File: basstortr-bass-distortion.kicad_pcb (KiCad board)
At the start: 2 copper layers, 50 x 80 mm, 48 parts, among them J1 Conn_01x04_Pin, J2 Conn_01x02_Pin, J3 Conn_01x02_Pin, Q1 BS170, Q2 BS170, Q3 BS170

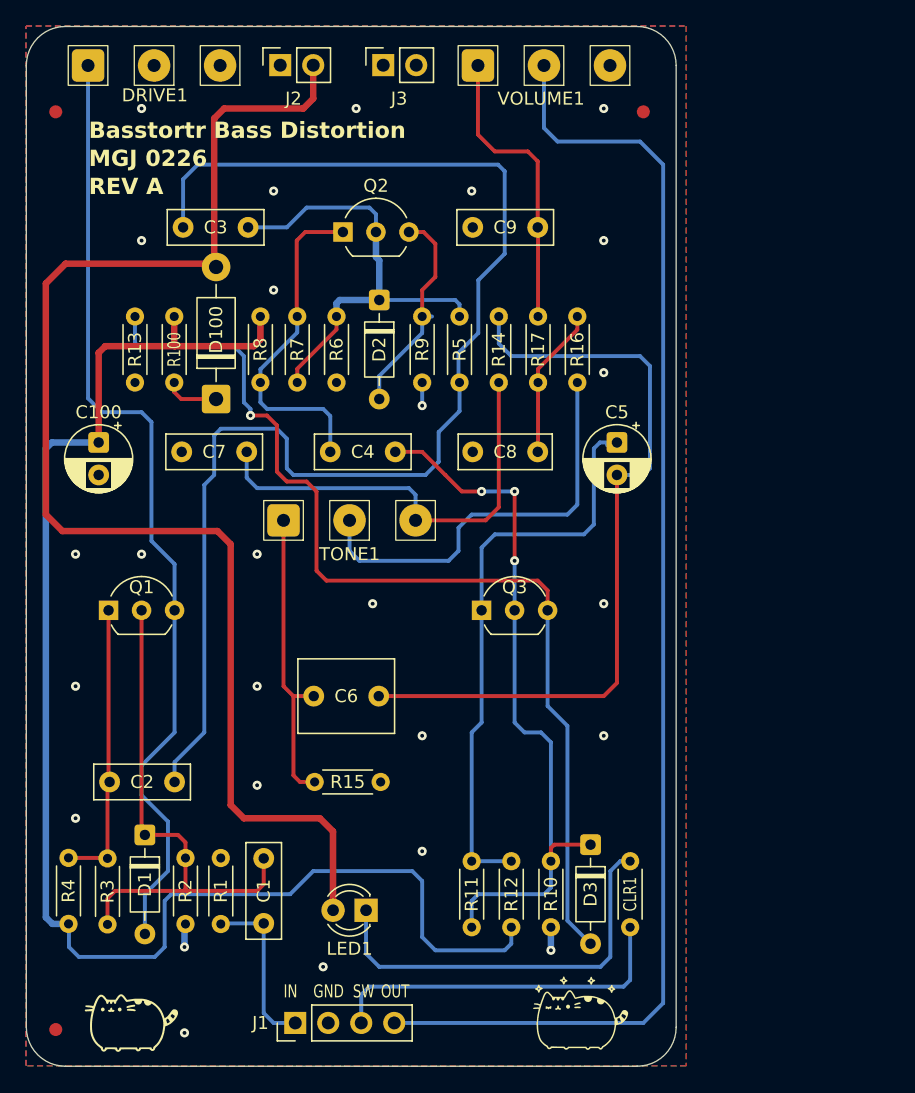
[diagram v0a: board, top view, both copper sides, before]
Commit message: RevB: New footprints and tracks
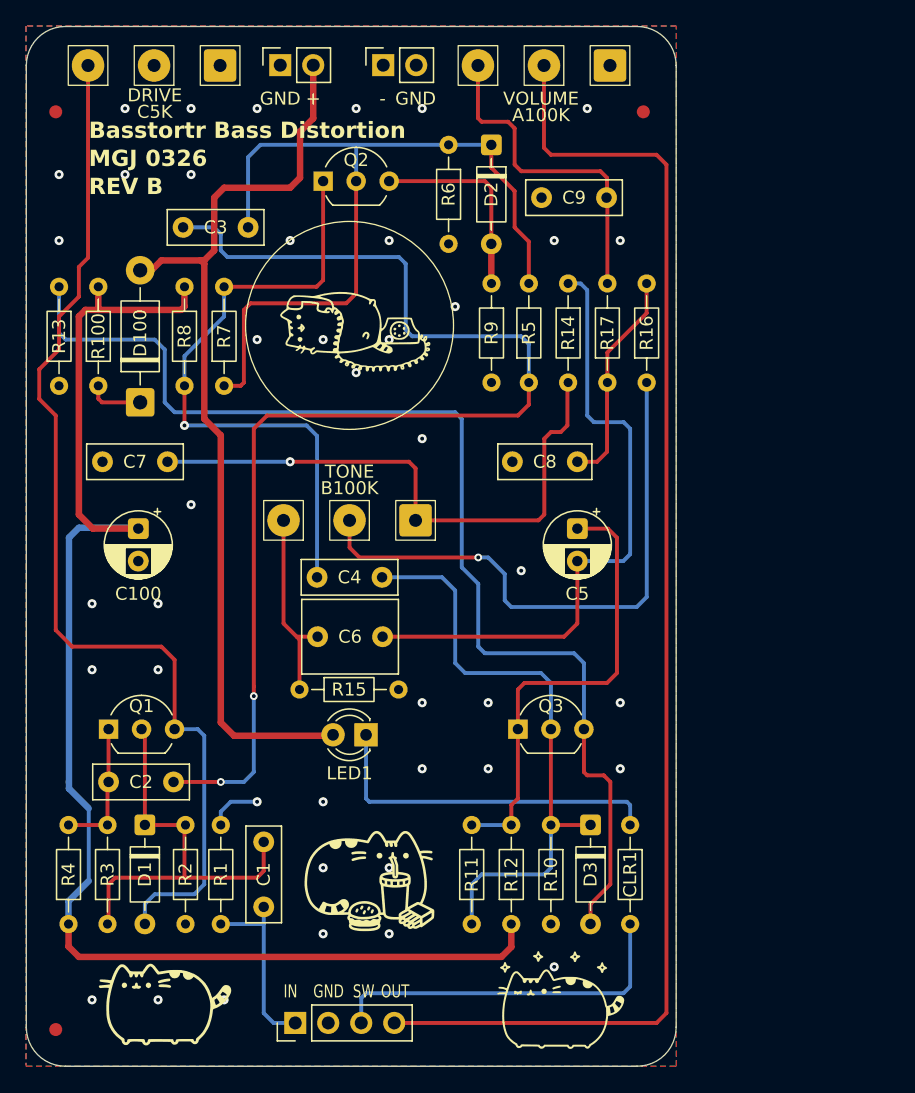
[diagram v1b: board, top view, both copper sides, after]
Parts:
- removed the G*** at (22.6, 90.1)
- removed the G*** at (57.1, 89.4)
- added G***: LOGO, LOGO, F.Cu at (40.9, 79.2)
- added G***: LOGO, LOGO, F.Cu at (39.9, 36.6)
- added G***: LOGO, LOGO, F.Cu at (55.6, 88.4)
- added G***: LOGO, LOGO, F.Cu at (25.1, 88.7)
- CLR1, R1, R10, R100, R11, R12, R13, R14, R15, R16, R17, R2, R3, R4, R5, R6, R7, R8, R9: footprint Resistor_THT:R_Axial_DIN0204_L3.6mm_D1.6mm_P5.08mm_Horizontal -> Resistor_THT:R_Axial_DIN0204_L3.6mm_D1.6mm_P7.62mm_Horizontal
- moved R6 15.8 mm to (47.0, 22.6)
- moved D2 14.7 mm to (50.3, 22.6)
- moved LED1 13.5 mm to (40.6, 68.0)
- moved C4 9.71 mm to (36.9, 55.9)
- moved Q3 9.56 mm to (52.3, 67.6)
- moved Q1 9.14 mm to (20.8, 67.6)
- moved C100 7.30 mm to (23.1, 52.1)
- moved C5 7.30 mm to (56.9, 52.1)
- moved R15 7.21 mm to (35.5, 64.5)
- moved R13 6.27 mm to (17.0, 33.5)
- moved R8 6.27 mm to (26.7, 33.5)
- moved C7 6.14 mm to (20.4, 47.0)
- moved R14 5.91 mm to (56.2, 33.3)
- moved R9 5.91 mm to (50.3, 33.3)
- moved D100 5.85 mm to (23.3, 42.4)
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- renumbered DRIVE1 to DRIVE, TONE1 to TONE, VOLUME1 to VOLUME
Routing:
- net /+: track 103.9 -> 72.0 mm
- net Net-(D2-K): track 35.4 -> 64.2 mm
- net Net-(Q2-D): track 26.0 -> 48.8 mm, vias 0 -> 1
- net Net-(R16-Pad1): track 32.4 -> 44.9 mm, vias 0 -> 1
- net Net-(Q1-D): track 22.2 -> 10.4 mm
- net Net-(C7-Pad2): track 33.9 -> 44.8 mm, vias 0 -> 1
- net Net-(C5-Pad2): track 59.8 -> 49.2 mm
- net Net-(D3-A): track 78.3 -> 88.6 mm, vias 1 -> 0
- net Net-(Q3-D): track 45.0 -> 35.6 mm
- net Net-(D3-K): track 55.5 -> 46.6 mm, vias 3 -> 0
- net Net-(C2-Pad2): track 102.3 -> 93.5 mm, vias 0 -> 2
- net Net-(D1-K): track 41.0 -> 32.4 mm
- net Net-(C6-Pad1): track 23.3 -> 15.1 mm
- net Net-(D1-A): track 74.0 -> 81.6 mm
- net VCC: track 113.6 -> 106.9 mm
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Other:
- board text added: "+"
- board text added: "-"
- board text added: "A100K"
- board text added: "B100K"
- board text added: "C5K"
- board text added: "MGJ 0326"
- board text added: "REV B"
- board text removed: "MGJ 0226"
- board text removed: "REV A"

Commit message: Rev C: Isolating parts to fit inside 125B
Fixed trace widths, trying to trace out signal on only one layer, changed component placement, etc..
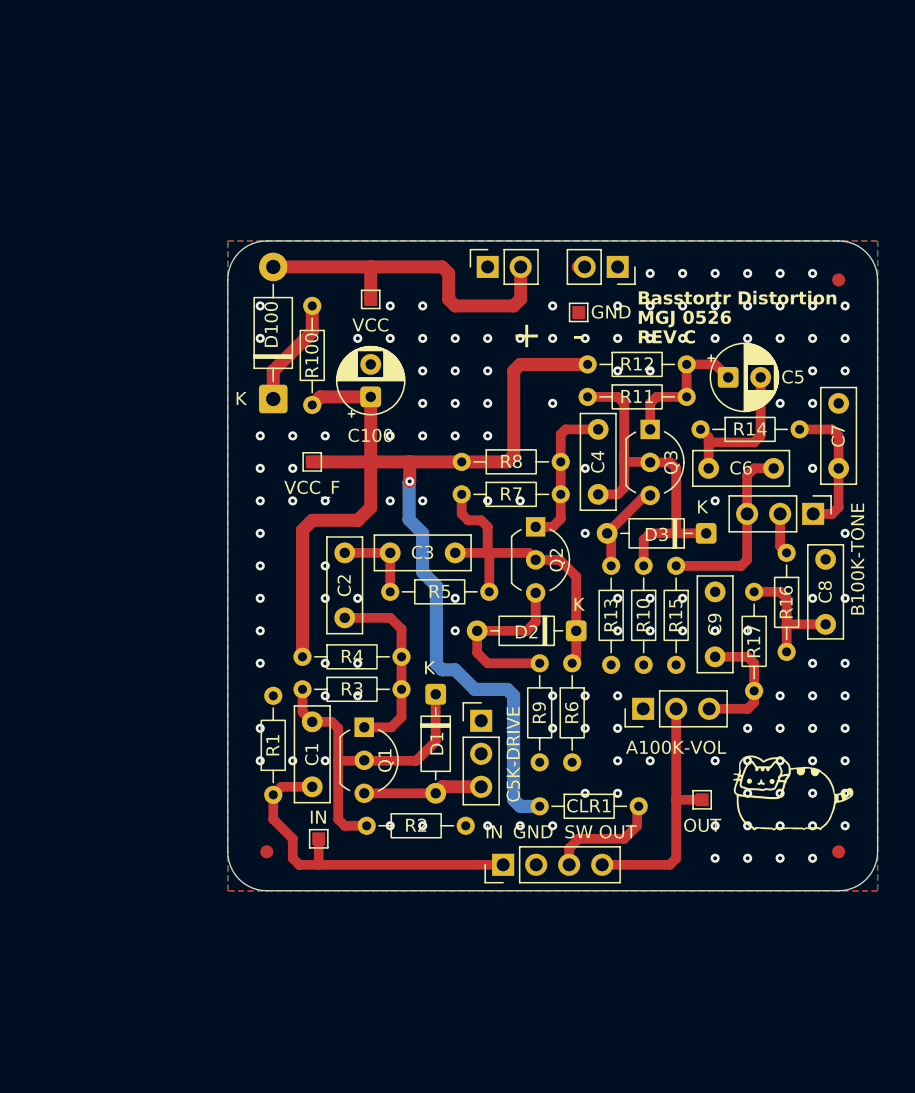
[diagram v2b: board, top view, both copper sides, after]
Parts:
- removed DRIVE: C5K, Potentiometer-THT-Alpha-16mm:Alpha-pot-16mm-5mm
- removed the G*** at (40.9, 79.2)
- removed the G*** at (39.9, 36.6)
- removed the G*** at (55.6, 88.4)
- removed the G*** at (25.1, 88.7)
- removed LED1: LED, LED_THT:LED_D3.0mm
- removed TONE: B100K, Potentiometer-THT-Alpha-16mm:Alpha-pot-16mm-5mm
- removed VOLUME: A100K, Potentiometer-THT-Alpha-16mm:Alpha-pot-16mm-5mm
- added G***: LOGO, LOGO, F.Cu at (73.5, 72.5)
- added POT1: C5K-DRIVE, Connector_PinHeader_2.54mm:PinHeader_1x03_P2.54mm_Vertical, F.Cu at (49.5, 66.9)
- added POT2: B100K-TONE, Connector_PinHeader_2.54mm:PinHeader_1x03_P2.54mm_Vertical, F.Cu at (75.0, 51.0)
- added POT3: A100K-VOL, Connector_PinHeader_2.54mm:PinHeader_1x03_P2.54mm_Vertical, F.Cu at (62.0, 66.0)
- added TP1: VCC, TestPoint:TestPoint_Pad_1.0x1.0mm, F.Cu at (41.0, 34.5)
- added TP2: VCC_F, TestPoint:TestPoint_Pad_1.0x1.0mm, F.Cu at (36.5, 47.0)
- added TP3: IN, TestPoint:TestPoint_Pad_1.0x1.0mm, F.Cu at (37.0, 76.0)
- added TP4: OUT, TestPoint:TestPoint_Pad_1.0x1.0mm, F.Cu at (66.5, 73.0)
- added TP5: GND, TestPoint:TestPoint_Pad_1.0x1.0mm, F.Cu at (57.0, 35.5)
- C6: footprint Capacitor_THT:C_Rect_L7.2mm_W5.5mm_P5.00mm_FKS2_FKP2_MKS2_MKP2 -> Capacitor_THT:C_Rect_L7.2mm_W2.5mm_P5.00mm_FKS2_FKP2_MKS2_MKP2
- moved FID2 82.9 mm to (77.0, 77.0)
- moved C7 56.8 mm to (77.0, 42.5), turned to -90 degrees
- moved R13 47.6 mm to (59.5, 55.0)
- moved R12 43.5 mm to (57.7, 39.5), turned to 0 degrees
- moved R11 41.5 mm to (57.7, 42.0), turned to 0 degrees
- moved R6 41.0 mm to (56.5, 62.5)
- moved D2 38.0 mm to (56.8, 60.0), turned to 180 degrees
- moved C6 37.4 mm to (72.0, 47.5), turned to 180 degrees
- moved C9 36.3 mm to (67.5, 62.0), turned to 90 degrees
- moved Q2 31.2 mm to (53.7, 52.0), turned to -90 degrees
- moved R15 30.5 mm to (64.5, 55.0), turned to -90 degrees
- moved C3 29.7 mm to (42.5, 54.0)
- moved R9 29.5 mm to (54.0, 62.5)
- moved R4 27.3 mm to (35.8, 62.0), turned to 0 degrees
- moved R8 25.2 mm to (48.0, 47.0), turned to 0 degrees
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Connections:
- net /+ renamed VCC+
- net /IN renamed IN
- net /SW renamed SW
- C100 pad 1: VCC -> VCC_F
- CLR1 pad 1: Net-(LED1-K) -> VCC_F
- J1 pad 4: /OUT -> OUT
- R100 pad 2: VCC -> VCC_F
- R12 pad 1: VCC -> VCC_F
- R4 pad 1: VCC -> VCC_F
- R8 pad 1: VCC -> VCC_F
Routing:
- net VCC: track 106.9 -> 0.00 mm
- net /OUT: track 102.8 -> 0.00 mm
- net VCC_F: track 0.00 -> 90.7 mm, vias 0 -> 1
- net Net-(C2-Pad2): track 93.5 -> 6.50 mm, vias 2 -> 0
- net Net-(D3-A): track 88.6 -> 7.15 mm
- net Net-(D1-A): track 81.6 -> 9.21 mm
- net VCC+: track 72.0 -> 26.6 mm
- net Net-(POT2-Pin_2): track 44.9 -> 3.21 mm, vias 1 -> 0
- net Net-(D2-K): track 64.2 -> 25.8 mm
- net Net-(C5-Pad2): track 49.2 -> 12.0 mm
- net Net-(Q2-D): track 48.8 -> 11.7 mm, vias 1 -> 0
- net Net-(POT2-Pin_1): track 44.8 -> 10.9 mm, vias 1 -> 0
- net Net-(LED1-K): track 27.0 -> 0.00 mm
- net Net-(Q3-D): track 35.6 -> 11.1 mm
- net OUT: track 0.00 -> 19.4 mm
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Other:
- board size 50 x 80 mm -> 50 x 50 mm
- board text added: "Basstortr Distortion"
- board text added: "MGJ 0526"
- board text added: "REV C"
- board text removed: "A100K"
- board text removed: "B100K"
- board text removed: "Basstortr Bass Distortion"
- board text removed: "C5K"
- board text removed: "MGJ 0326"
- board text removed: "REV B"
